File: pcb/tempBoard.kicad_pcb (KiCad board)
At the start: 2 copper layers, 33.3 x 66.1 mm, 13 parts, among them J1 OLED_128X64_1.3_I2C, U1 SHTC3, U2 XIAO-RP2040-DIP

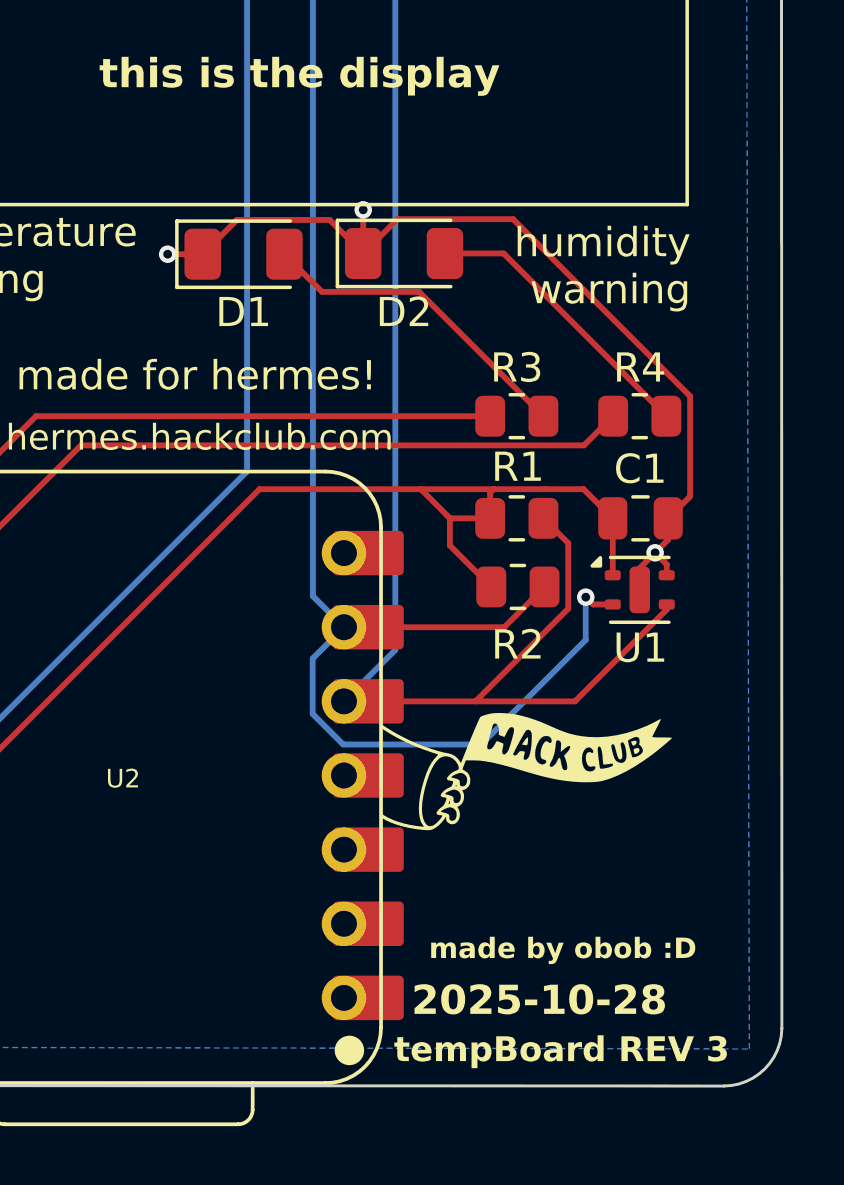
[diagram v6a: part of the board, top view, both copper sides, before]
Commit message: make jlc cheaper
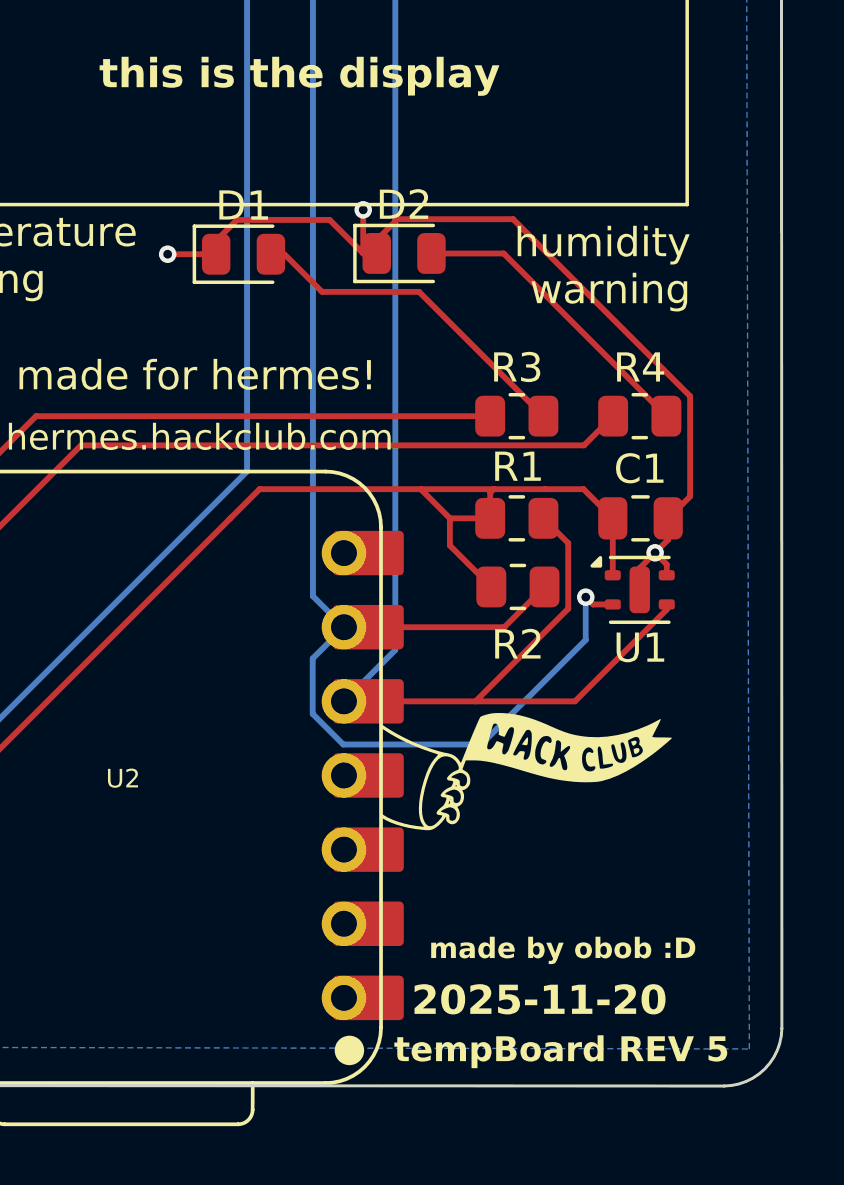
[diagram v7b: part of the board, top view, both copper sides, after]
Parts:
- D1: footprint LED_SMD:LED_1206_3216Metric -> LED_SMD:LED_0805_2012Metric
- D2: value LED_BLUE -> LED_GREEN; footprint LED_SMD:LED_1206_3216Metric -> LED_SMD:LED_0805_2012Metric
- R3: value 68 -> 47
- R4: value 33 -> 200
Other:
- board text added: "2025-11-20"
- board text added: "tempBoard REV 5"
- board text removed: "2025-10-28"
- board text removed: "tempBoard REV 3"
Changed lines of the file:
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@@
 	(net 23 "TEMP")
 	(net 24 "HUM")
-	(footprint "LED_SMD:LED_1206_3216Metric"
+	(footprint "LED_SMD:LED_0805_2012Metric"
 		(layer "F.Cu")
 		(at 164.7 87.2)
-		(descr "LED SMD 1206 (3216 Metric), square (rectangular) end terminal, IPC_7351 nominal, (Body size source: http://www.tortai-tech.com/upload/download/2011102023233369053.pdf), generated with kicad-footprint-generator")
+		(descr "LED SMD 0805 (2012 Metric), square (rectangular) end terminal, IPC_7351 nominal, (Body size source: https://docs.google.com/spreadsheets/d/1BsfQQcO9C6DZCsRaXUlFlo91Tg2WpOkGARC1WS5S8t0/edit?usp=sharing), generated with kicad-footprint-generator")
 		(tags "LED")
 		(property "Reference" "D1"
-			(at 0 2 0)
+			(at 0 -1.65 0)
 			(layer "F.SilkS")
 			(effects
@@
 		)
 		(property "Value" "LED_RED"
-			(at 0 1.82 0)
+			(at 0 1.65 0)
 			(layer "F.Fab")
 			(effects
@@
 			)
 		)
-		(property "Footprint" "LED_SMD:LED_1206_3216Metric"
+		(property "Footprint" "LED_SMD:LED_0805_2012Metric"
 			(at 0 0 0)
 			(unlocked yes)
@@
 			)
 		)
-		(property "LCSC" "C965822"
+		(property "LCSC" "C84256"
 			(at 0 0 0)
 			(unlocked yes)
@@
 		(attr smd)
 		(fp_line
-			(start -2.285 -1.135)
-			(end -2.285 1.135)
+			(start -1.685 -0.96)
+			(end -1.685 0.96)
 			(stroke
 				(width 0.12)
@@
 		)
 		(fp_line
-			(start -2.285 1.135)
-			(end 1.6 1.135)
+			(start -1.685 0.96)
+			(end 1 0.96)
 			(stroke
 				(width 0.12)
@@
 		)
 		(fp_line
-			(start 1.6 -1.135)
-			(end -2.285 -1.135)
+			(start 1 -0.96)
+			(end -1.685 -0.96)
 			(stroke
 				(width 0.12)
@@
 		)
 		(fp_line
-			(start -2.28 -1.12)
-			(end 2.28 -1.12)
+			(start -1.68 -0.95)
+			(end 1.68 -0.95)
 			(stroke
 				(width 0.05)
@@
 		)
 		(fp_line
-			(start -2.28 1.12)
-			(end -2.28 -1.12)
+			(start -1.68 0.95)
+			(end -1.68 -0.95)
 			(stroke
 				(width 0.05)
@@
 		)
 		(fp_line
-			(start 2.28 -1.12)
-			(end 2.28 1.12)
+			(start 1.68 -0.95)
+			(end 1.68 0.95)
 			(stroke
 				(width 0.05)
@@
 		)
 		(fp_line
-			(start 2.28 1.12)
-			(end -2.28 1.12)
+			(start 1.68 0.95)
+			(end -1.68 0.95)
 			(stroke
 				(width 0.05)
@@
 		)
 		(fp_line
-			(start -1.6 -0.4)
-			(end -1.6 0.8)
+			(start -1 -0.3)
+			(end -1 0.6)
 			(stroke
 				(width 0.1)
@@
 		)
 		(fp_line
-			(start -1.6 0.8)
-			(end 1.6 0.8)
+			(start -1 0.6)
+			(end 1 0.6)
 			(stroke
 				(width 0.1)
@@
 		)
 		(fp_line
-			(start -1.2 -0.8)
-			(end -1.6 -0.4)
+			(start -0.7 -0.6)
+			(end -1 -0.3)
 			(stroke
 				(width 0.1)
@@
 		)
 		(fp_line
-			(start 1.6 -0.8)
-			(end -1.2 -0.8)
+			(start 1 -0.6)
+			(end -0.7 -0.6)
 			(stroke
 				(width 0.1)
@@
 		)
 		(fp_line
-			(start 1.6 0.8)
-			(end 1.6 -0.8)
+			(start 1 0.6)
+			(end 1 -0.6)
 			(stroke
 				(width 0.1)
@@
 			(effects
 				(font
-					(size 0.8 0.8)
-					(thickness 0.12)
+					(size 0.5 0.5)
+					(thickness 0.08)
 				)
 			)
 		)
 		(pad "1" smd roundrect
-			(at -1.4 0)
-			(size 1.25 1.75)
+			(at -0.9375 0)
+			(size 0.975 1.4)
 			(layers "F.Cu" "F.Paste" "F.Mask")
-			(roundrect_rratio 0.2)
+			(roundrect_rratio 0.25)
 			(net 1 "GND")
 			(pinfunction "K")
@@
 		)
 		(pad "2" smd roundrect
-			(at 1.4 0)
-			(size 1.25 1.75)
+			(at 0.9375 0)
+			(size 0.975 1.4)
 			(layers "F.Cu" "F.Paste" "F.Mask")
-			(roundrect_rratio 0.2)
+			(roundrect_rratio 0.25)
 			(net 21 "Net-(D1-A)")
 			(pinfunction "A")
 			(pintype "passive")
 		)
-		(model "${KICAD8_3DMODEL_DIR}/LED_SMD.3dshapes/LED_1206_3216Metric.wrl"
+		(model "${KICAD8_3DMODEL_DIR}/LED_SMD.3dshapes/LED_0805_2012Metric.wrl"
 			(offset
 				(xyz 0 0 0)
@@
 		(sheetname "Root")
 		(sheetfile "tempBoard.kicad_sch")
-		(attr through_hole exclude_from_pos_files)
+		(attr through_hole exclude_from_pos_files dnp)
 		(fp_line
 			(start -13.4 -12.3)
@@
 		)
 	)
-	(footprint "LED_SMD:LED_1206_3216Metric"
+	(footprint "LED_SMD:LED_0805_2012Metric"
 		(layer "F.Cu")
 		(at 170.2 87.175)
-		(descr "LED SMD 1206 (3216 Metric), square (rectangular) end terminal, IPC_7351 nominal, (Body size source: http://www.tortai-tech.com/upload/download/2011102023233369053.pdf), generated with kicad-footprint-generator")
+		(descr "LED SMD 0805 (2012 Metric), square (rectangular) end terminal, IPC_7351 nominal, (Body size source: https://docs.google.com/spreadsheets/d/1BsfQQcO9C6DZCsRaXUlFlo91Tg2WpOkGARC1WS5S8t0/edit?usp=sharing), generated with kicad-footprint-generator")
 		(tags "LED")
 		(property "Reference" "D2"
-			(at 0 2.025 0)
+			(at 0 -1.65 0)
 			(layer "F.SilkS")
 			(effects
@@
 			)
 		)
-		(property "Value" "LED_BLUE"
-			(at 0 1.82 0)
+		(property "Value" "LED_GREEN"
+			(at 0 1.65 0)
 			(layer "F.Fab")
 			(effects
@@
 			)
 		)
-		(property "Footprint" "LED_SMD:LED_1206_3216Metric"
+		(property "Footprint" "LED_SMD:LED_0805_2012Metric"
 			(at 0 0 0)
 			(unlocked yes)
@@
 			)
 		)
-		(property "LCSC" "C28310438"
+		(property "LCSC" "C2297"
 			(at 0 0 0)
 			(unlocked yes)
@@
 		(attr smd)
 		(fp_line
-			(start -2.285 -1.135)
-			(end -2.285 1.135)
+			(start -1.685 -0.96)
+			(end -1.685 0.96)
 			(stroke
 				(width 0.12)
@@
 		)
 		(fp_line
-			(start -2.285 1.135)
-			(end 1.6 1.135)
+			(start -1.685 0.96)
+			(end 1 0.96)
 			(stroke
 				(width 0.12)
@@
 		)
 		(fp_line
-			(start 1.6 -1.135)
-			(end -2.285 -1.135)
+			(start 1 -0.96)
+			(end -1.685 -0.96)
 			(stroke
 				(width 0.12)
@@
 		)
 		(fp_line
-			(start -2.28 -1.12)
-			(end 2.28 -1.12)
+			(start -1.68 -0.95)
+			(end 1.68 -0.95)
 			(stroke
 				(width 0.05)
@@
 		)
 		(fp_line
-			(start -2.28 1.12)
-			(end -2.28 -1.12)
+			(start -1.68 0.95)
+			(end -1.68 -0.95)
 			(stroke
 				(width 0.05)
@@
 		)
 		(fp_line
-			(start 2.28 -1.12)
-			(end 2.28 1.12)
+			(start 1.68 -0.95)
+			(end 1.68 0.95)
 			(stroke
 				(width 0.05)
@@
 		)
 		(fp_line
-			(start 2.28 1.12)
-			(end -2.28 1.12)
+			(start 1.68 0.95)
+			(end -1.68 0.95)
 			(stroke
 				(width 0.05)
@@
 		)
 		(fp_line
-			(start -1.6 -0.4)
-			(end -1.6 0.8)
+			(start -1 -0.3)
+			(end -1 0.6)
 			(stroke
 				(width 0.1)
@@
 		)
 		(fp_line
-			(start -1.6 0.8)
-			(end 1.6 0.8)
+			(start -1 0.6)
+			(end 1 0.6)
 			(stroke
 				(width 0.1)
@@
 		)
 		(fp_line
-			(start -1.2 -0.8)
-			(end -1.6 -0.4)
+			(start -0.7 -0.6)
+			(end -1 -0.3)
 			(stroke
 				(width 0.1)
@@
 		)
 		(fp_line
-			(start 1.6 -0.8)
-			(end -1.2 -0.8)
+			(start 1 -0.6)
+			(end -0.7 -0.6)
 			(stroke
 				(width 0.1)
@@
 		)
 		(fp_line
-			(start 1.6 0.8)
-			(end 1.6 -0.8)
+			(start 1 0.6)
+			(end 1 -0.6)
 			(stroke
 				(width 0.1)
@@
 			(effects
 				(font
-					(size 0.8 0.8)
-					(thickness 0.12)
+					(size 0.5 0.5)
+					(thickness 0.08)
 				)
 			)
 		)
 		(pad "1" smd roundrect
-			(at -1.4 0)
-			(size 1.25 1.75)
+			(at -0.9375 0)
+			(size 0.975 1.4)
 			(layers "F.Cu" "F.Paste" "F.Mask")
-			(roundrect_rratio 0.2)
+			(roundrect_rratio 0.25)
 			(net 1 "GND")
 			(pinfunction "K")
@@
 		)
 		(pad "2" smd roundrect
-			(at 1.4 0)
-			(size 1.25 1.75)
+			(at 0.9375 0)
+			(size 0.975 1.4)
 			(layers "F.Cu" "F.Paste" "F.Mask")
-			(roundrect_rratio 0.2)
+			(roundrect_rratio 0.25)
 			(net 22 "Net-(D2-A)")
 			(pinfunction "A")
 			(pintype "passive")
 		)
-		(model "${KICAD8_3DMODEL_DIR}/LED_SMD.3dshapes/LED_1206_3216Metric.wrl"
+		(model "${KICAD8_3DMODEL_DIR}/LED_SMD.3dshapes/LED_0805_2012Metric.wrl"
 			(offset
 				(xyz 0 0 0)
@@
 		(sheetname "Root")
 		(sheetfile "tempBoard.kicad_sch")
-		(attr smd exclude_from_pos_files)
+		(attr smd exclude_from_pos_files dnp)
 		(fp_line
 			(start 8.89 8.509)
@@
 		(tags "resistor")
 		(property "Reference" "R1"
-			(at -0.0375 1.75 360)
+			(at -0.0375 1.75 0)
 			(layer "F.SilkS")
 			(effects
@@
 		)
 		(property "Value" "4k7"
-			(at 0 1.65 360)
+			(at 0 1.65 0)
 			(layer "F.Fab")
 			(effects
@@
 		)
 		(fp_text user "${REFERENCE}"
-			(at 0 0 360)
+			(at 0 0 0)
 			(layer "F.Fab")
 			(effects
@@
 			)
 		)
-		(property "Value" "68"
+		(property "Value" "47"
 			(at 0 1.65 0)
 			(layer "F.Fab")
@@
 			)
 		)
-		(property "LCSC" "C17802"
+		(property "LCSC" "C17714"
 			(at 0 0 0)
 			(unlocked yes)
@@
 			)
 		)
-		(property "Value" "33"
+		(property "Value" "200"
 			(at 0 1.65 0)
 			(layer "F.Fab")
@@
 			)
 		)
-		(property "LCSC" "C17634"
+		(property "LCSC" "C17540"
 			(at 0 0 0)
 			(unlocked yes)
@@
 		)
 	)
-	(gr_text "tempBoard REV 3"
+	(gr_text "tempBoard REV 5"
 		(at 169.85 114.95 0)
 		(layer "F.SilkS")
@@
 		)
 	)
-	(gr_text "2025-10-28"
+	(gr_text "2025-11-20"
 		(at 170.45 113.35 0)
 		(layer "F.SilkS")
